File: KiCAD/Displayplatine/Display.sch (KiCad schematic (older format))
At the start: 13 parts

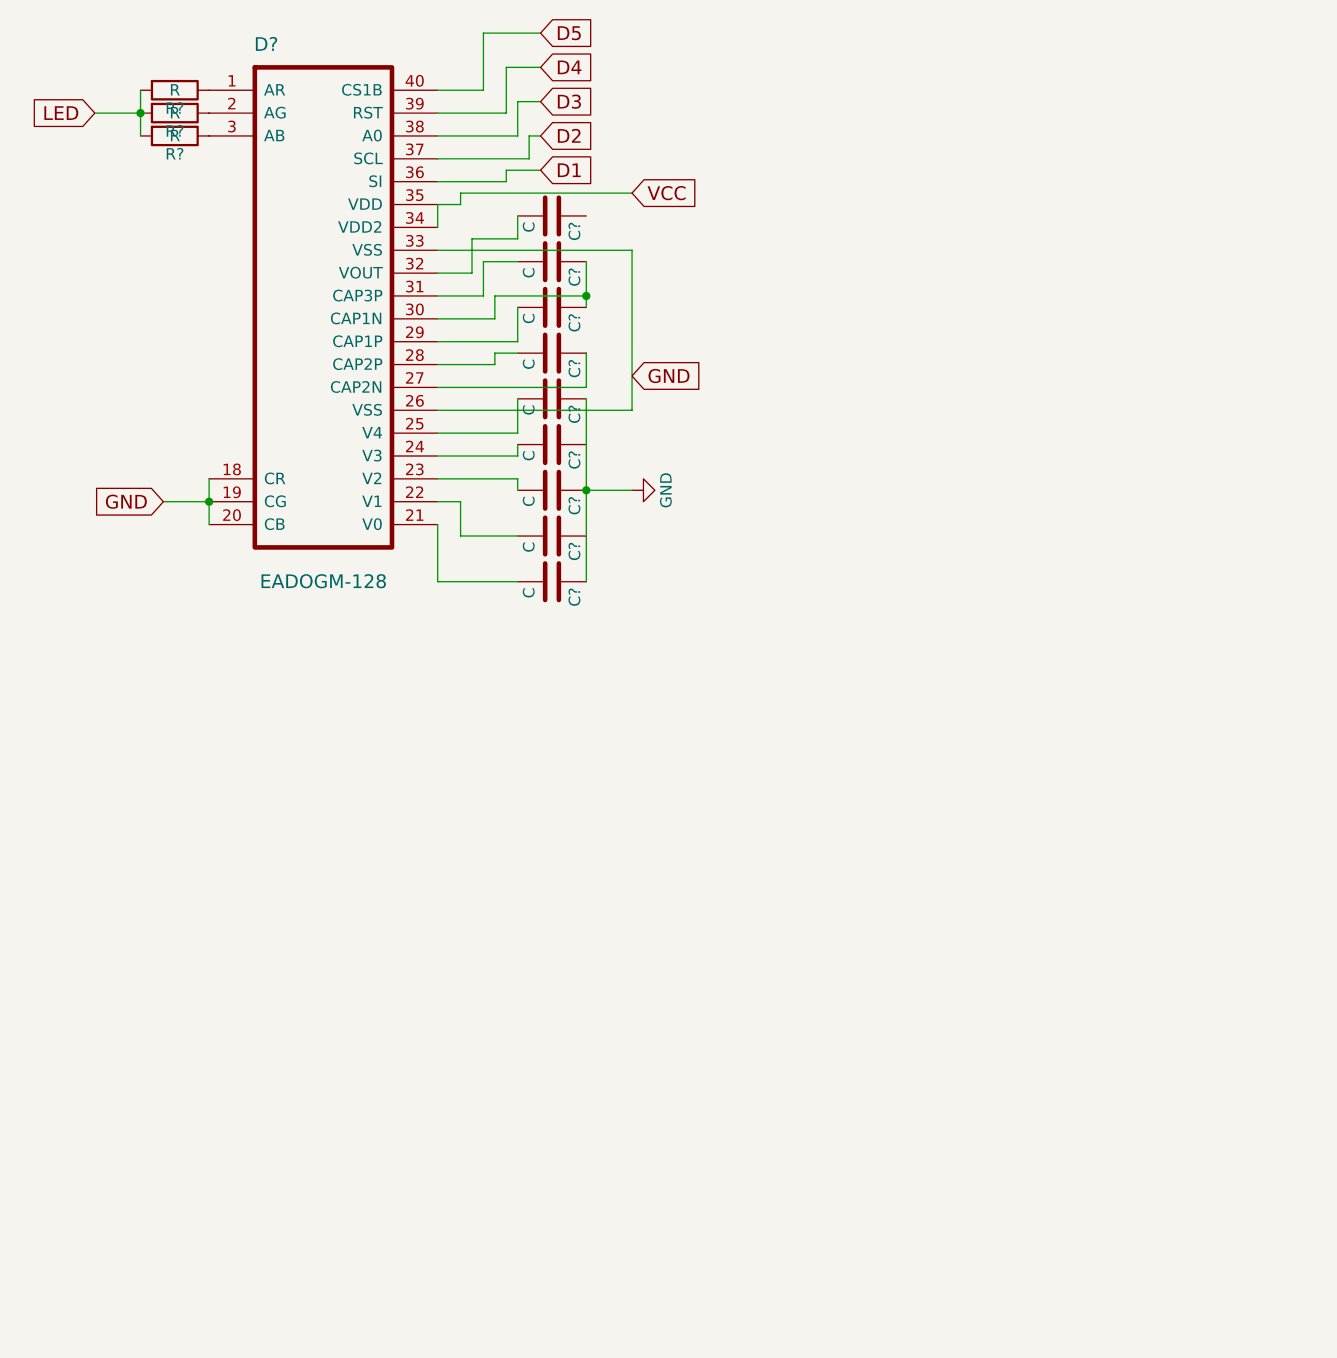
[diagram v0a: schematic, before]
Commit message: Footprints auf Displayplatine zugeordnet
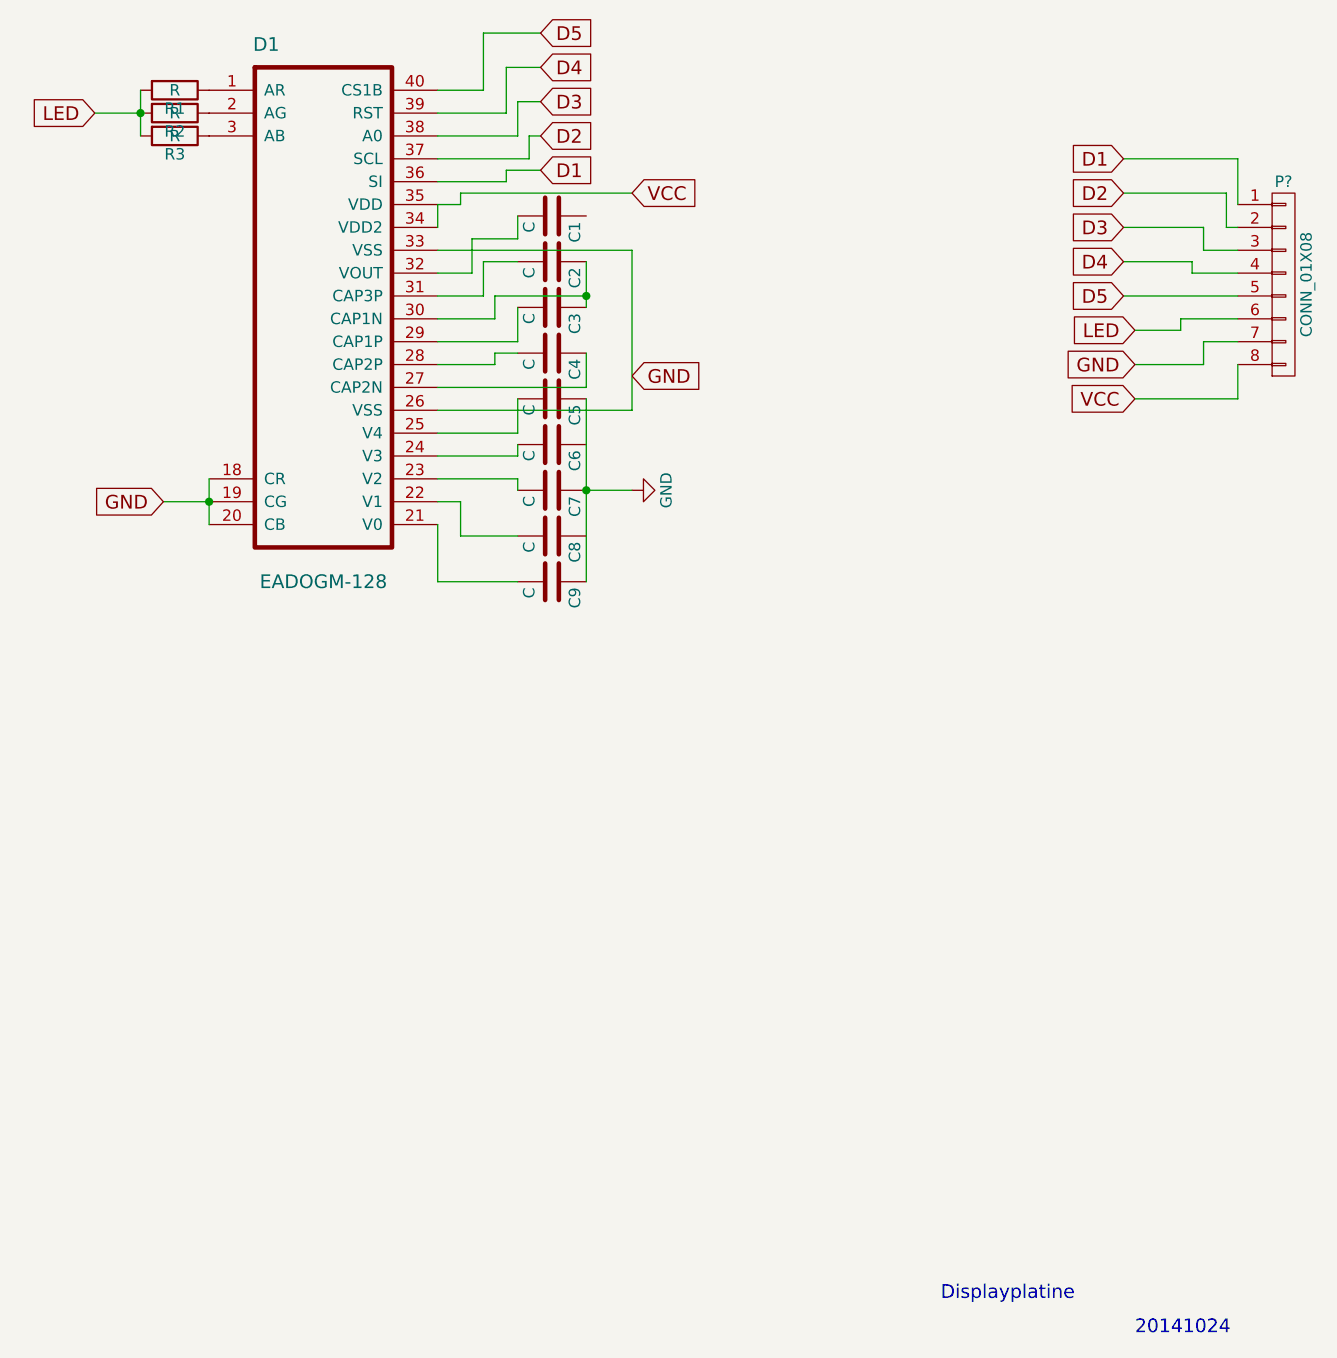
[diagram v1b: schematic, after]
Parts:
- added P?: CONN_01X08, symbol CONN_01X08
- gave numbers to parts that had none: 13
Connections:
- net D1: now also P?.1 (P1)
- net D2: now also P?.2 (P2)
- net D3: now also P?.3 (P3)
- net D4: now also P?.4 (P4)
- net D5: now also P?.5 (P5)
- net GND: now also P?.7 (P7)
- net LED: now also P?.6 (P6)
- net VCC: now also P?.8 (P8)
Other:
- note added: "20141024"
- note added: "Displayplatine"
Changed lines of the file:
@@
 LIBS:contrib
 LIBS:valves
+LIBS:Display-cache
 EELAYER 25 0
 EELAYER END
@@
 $EndDescr
 $Comp
-L EADOGM-128 D?
+L EADOGM-128 D1
 U 1 1 562B6F62
 P 4700 2800
-F 0 "D?" H 4450 3600 60  0000 C CNN
+F 0 "D1" H 4450 3600 60  0000 C CNN
 F 1 "EADOGM-128" H 4700 1250 60  0000 C CNN
 F 2 "" H 4450 3600 60  0000 C CNN
@@
 $EndComp
 $Comp
-L R R?
+L R R1
 U 1 1 562B7228
 P 4050 2200
-F 0 "R?" V 4130 2200 50  0000 C CNN
+F 0 "R1" V 4130 2200 50  0000 C CNN
 F 1 "R" V 4050 2200 50  0000 C CNN
 F 2 "" V 3980 2200 30  0000 C CNN
@@
 $EndComp
 $Comp
-L R R?
+L R R2
 U 1 1 562B727B
 P 4050 2300
-F 0 "R?" V 4130 2300 50  0000 C CNN
+F 0 "R2" V 4130 2300 50  0000 C CNN
 F 1 "R" V 4050 2300 50  0000 C CNN
 F 2 "" V 3980 2300 30  0000 C CNN
@@
 $EndComp
 $Comp
-L R R?
+L R R3
 U 1 1 562B72AC
 P 4050 2400
-F 0 "R?" V 4130 2400 50  0000 C CNN
+F 0 "R3" V 4130 2400 50  0000 C CNN
 F 1 "R" V 4050 2400 50  0000 C CNN
 F 2 "" V 3980 2400 30  0000 C CNN
@@
 $EndComp
 $Comp
-L C C?
+L C C9
 U 1 1 562B74C8
 P 5700 4350
-F 0 "C?" H 5725 4450 50  0000 L CNN
+F 0 "C9" H 5725 4450 50  0000 L CNN
 F 1 "C" H 5725 4250 50  0000 L CNN
 F 2 "" H 5738 4200 30  0000 C CNN
@@
 $EndComp
 $Comp
-L C C?
+L C C8
 U 1 1 562B7536
 P 5700 4150
-F 0 "C?" H 5725 4250 50  0000 L CNN
+F 0 "C8" H 5725 4250 50  0000 L CNN
 F 1 "C" H 5725 4050 50  0000 L CNN
 F 2 "" H 5738 4000 30  0000 C CNN
@@
 $EndComp
 $Comp
-L C C?
+L C C7
 U 1 1 562B75A3
 P 5700 3950
-F 0 "C?" H 5725 4050 50  0000 L CNN
+F 0 "C7" H 5725 4050 50  0000 L CNN
 F 1 "C" H 5725 3850 50  0000 L CNN
 F 2 "" H 5738 3800 30  0000 C CNN
@@
 $EndComp
 $Comp
-L C C?
+L C C6
 U 1 1 562B75CA
 P 5700 3750
-F 0 "C?" H 5725 3850 50  0000 L CNN
+F 0 "C6" H 5725 3850 50  0000 L CNN
 F 1 "C" H 5725 3650 50  0000 L CNN
 F 2 "" H 5738 3600 30  0000 C CNN
@@
 $EndComp
 $Comp
-L C C?
+L C C5
 U 1 1 562B7621
 P 5700 3550
-F 0 "C?" H 5725 3650 50  0000 L CNN
+F 0 "C5" H 5725 3650 50  0000 L CNN
 F 1 "C" H 5725 3450 50  0000 L CNN
 F 2 "" H 5738 3400 30  0000 C CNN
@@
 $EndComp
 $Comp
-L GND #PWR?
+L GND #PWR01
 U 1 1 562B7704
 P 6050 3950
-F 0 "#PWR?" H 6050 3700 50  0001 C CNN
+F 0 "#PWR01" H 6050 3700 50  0001 C CNN
 F 1 "GND" H 6050 3800 50  0000 C CNN
 F 2 "" H 6050 3950 60  0000 C CNN
@@
 $EndComp
 $Comp
-L C C?
+L C C4
 U 1 1 562B7CE7
 P 5700 3350
-F 0 "C?" H 5725 3450 50  0000 L CNN
+F 0 "C4" H 5725 3450 50  0000 L CNN
 F 1 "C" H 5725 3250 50  0000 L CNN
 F 2 "" H 5738 3200 30  0000 C CNN
@@
 $EndComp
 $Comp
-L C C?
+L C C3
 U 1 1 562B7D68
 P 5700 3150
-F 0 "C?" H 5725 3250 50  0000 L CNN
+F 0 "C3" H 5725 3250 50  0000 L CNN
 F 1 "C" H 5725 3050 50  0000 L CNN
 F 2 "" H 5738 3000 30  0000 C CNN
@@
 $EndComp
 $Comp
-L C C?
+L C C2
 U 1 1 562B7DB9
 P 5700 2950
-F 0 "C?" H 5725 3050 50  0000 L CNN
+F 0 "C2" H 5725 3050 50  0000 L CNN
 F 1 "C" H 5725 2850 50  0000 L CNN
 F 2 "" H 5738 2800 30  0000 C CNN
@@
 $EndComp
 $Comp
-L C C?
+L C C1
 U 1 1 562B7EAB
 P 5700 2750
-F 0 "C?" H 5725 2850 50  0000 L CNN
+F 0 "C1" H 5725 2850 50  0000 L CNN
 F 1 "C" H 5725 2650 50  0000 L CNN
 F 2 "" H 5738 2600 30  0000 C CNN
@@
 Wire Wire Line
 	5200 2900 6050 2900
+$Comp
+L CONN_01X08 P?
+U 1 1 562B950F
+P 8900 3050
+F 0 "P?" H 8900 3500 50  0000 C CNN
+F 1 "CONN_01X08" V 9000 3050 50  0000 C CNN
+F 2 "" H 8900 3050 60  0000 C CNN
+F 3 "" H 8900 3050 60  0000 C CNN
+	1    8900 3050
+	1    0    0    -1
+$EndComp
+Text GLabel 8200 2500 0    60   Input ~ 0
+D1
+Text GLabel 8200 2650 0    60   Input ~ 0
+D2
+Text GLabel 8200 2800 0    60   Input ~ 0
+D3
+Text GLabel 8200 2950 0    60   Input ~ 0
+D4
+Text GLabel 8200 3100 0    60   Input ~ 0
+D5
+Text GLabel 8250 3250 0    60   Input ~ 0
+LED
+Text GLabel 8250 3400 0    60   Input ~ 0
+GND
+Text GLabel 8250 3550 0    60   Input ~ 0
+VCC
+Wire Wire Line
+	8200 2500 8700 2500
+Wire Wire Line
+	8700 2500 8700 2700
+Wire Wire Line
+	8200 2650 8650 2650
+Wire Wire Line
+	8650 2650 8650 2800
+Wire Wire Line
+	8650 2800 8700 2800
+Wire Wire Line
+	8200 2800 8550 2800
+Wire Wire Line
+	8550 2800 8550 2900
+Wire Wire Line
+	8550 2900 8700 2900
+Wire Wire Line
+	8200 2950 8500 2950
+Wire Wire Line
+	8500 2950 8500 3000
+Wire Wire Line
+	8500 3000 8700 3000
+Wire Wire Line
+	8200 3100 8700 3100
+Wire Wire Line
+	8250 3250 8450 3250
+Wire Wire Line
+	8450 3250 8450 3200
+Wire Wire Line
+	8450 3200 8700 3200
+Wire Wire Line
+	8250 3400 8550 3400
+Wire Wire Line
+	8550 3400 8550 3300
+Wire Wire Line
+	8550 3300 8700 3300
+Wire Wire Line
+	8250 3550 8700 3550
+Wire Wire Line
+	8700 3550 8700 3400
+Text Notes 7400 7500 0    60   ~ 0
+Displayplatine
+Text Notes 8250 7650 0    60   ~ 0
+20141024
 $EndSCHEMATC

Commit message: Footprint EADOG korrigiert + Kondensatoren besserer Footprint
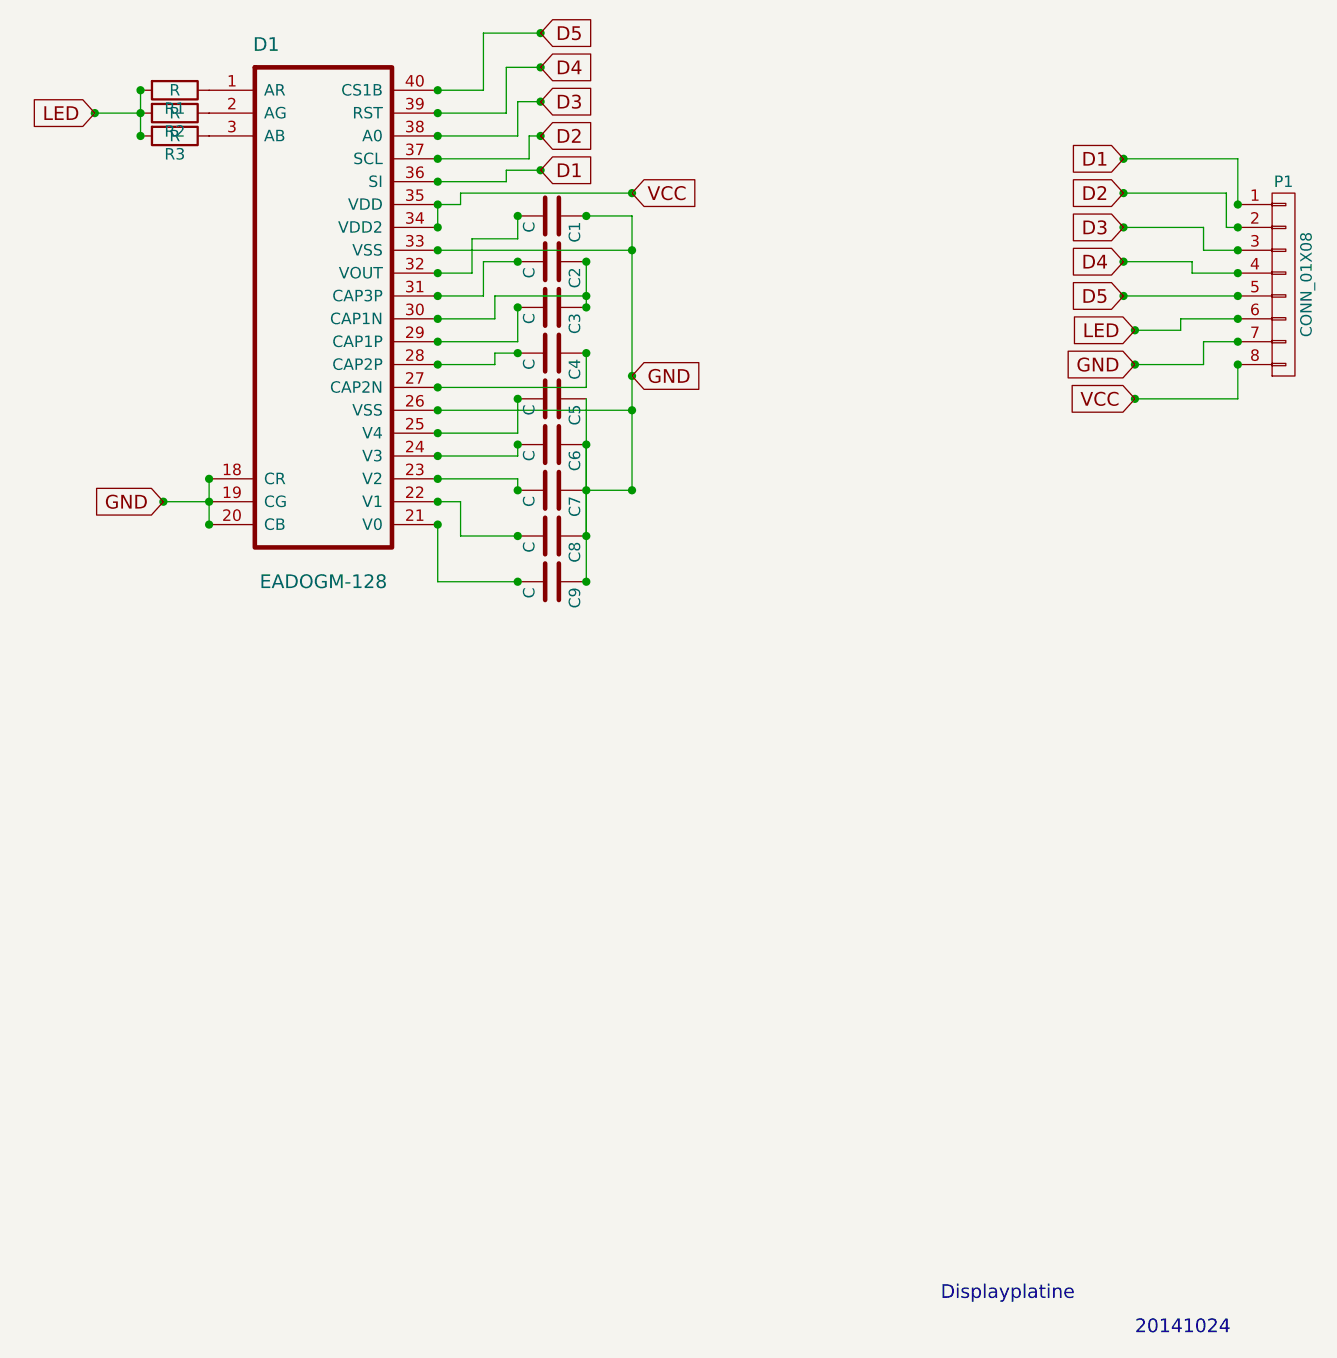
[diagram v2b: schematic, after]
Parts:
- C1, C2, C3, C4, C5, C6, C7, C8, C9: footprint (none) -> Capacitors_ThroughHole:C_Disc_D3_P2.5
- D1: footprint (none) -> Displayplatine:EADOG128
- P1: renamed from P?; footprint (none) -> Pin_Headers:Pin_Header_Straight_1x08
- R1, R2, R3: footprint (none) -> Resistors_ThroughHole:Resistor_Horizontal_RM10mm
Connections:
- net GND: now also C1.1, C6.1, C8.1
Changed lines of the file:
@@
 F 0 "D1" H 4450 3600 60  0000 C CNN
 F 1 "EADOGM-128" H 4700 1250 60  0000 C CNN
-F 2 "" H 4450 3600 60  0000 C CNN
+F 2 "Displayplatine:EADOG128" H 4450 3600 60  0001 C CNN
 F 3 "" H 4450 3600 60  0000 C CNN
 	1    4700 2800
@@
 F 0 "R1" V 4130 2200 50  0000 C CNN
 F 1 "R" V 4050 2200 50  0000 C CNN
-F 2 "" V 3980 2200 30  0000 C CNN
+F 2 "Resistors_ThroughHole:Resistor_Horizontal_RM10mm" V 3980 2200 30  0001 C CNN
 F 3 "" H 4050 2200 30  0000 C CNN
 	1    4050 2200
@@
 F 0 "R2" V 4130 2300 50  0000 C CNN
 F 1 "R" V 4050 2300 50  0000 C CNN
-F 2 "" V 3980 2300 30  0000 C CNN
+F 2 "Resistors_ThroughHole:Resistor_Horizontal_RM10mm" V 3980 2300 30  0001 C CNN
 F 3 "" H 4050 2300 30  0000 C CNN
 	1    4050 2300
@@
 F 0 "R3" V 4130 2400 50  0000 C CNN
 F 1 "R" V 4050 2400 50  0000 C CNN
-F 2 "" V 3980 2400 30  0000 C CNN
+F 2 "Resistors_ThroughHole:Resistor_Horizontal_RM10mm" V 3980 2400 30  0001 C CNN
 F 3 "" H 4050 2400 30  0000 C CNN
 	1    4050 2400
@@
 F 0 "C9" H 5725 4450 50  0000 L CNN
 F 1 "C" H 5725 4250 50  0000 L CNN
-F 2 "" H 5738 4200 30  0000 C CNN
+F 2 "Capacitors_ThroughHole:C_Disc_D3_P2.5" H 5738 4200 30  0001 C CNN
 F 3 "" H 5700 4350 60  0000 C CNN
 	1    5700 4350
@@
 F 0 "C8" H 5725 4250 50  0000 L CNN
 F 1 "C" H 5725 4050 50  0000 L CNN
-F 2 "" H 5738 4000 30  0000 C CNN
+F 2 "Capacitors_ThroughHole:C_Disc_D3_P2.5" H 5738 4000 30  0001 C CNN
 F 3 "" H 5700 4150 60  0000 C CNN
 	1    5700 4150
@@
 F 0 "C7" H 5725 4050 50  0000 L CNN
 F 1 "C" H 5725 3850 50  0000 L CNN
-F 2 "" H 5738 3800 30  0000 C CNN
+F 2 "Capacitors_ThroughHole:C_Disc_D3_P2.5" H 5738 3800 30  0001 C CNN
 F 3 "" H 5700 3950 60  0000 C CNN
 	1    5700 3950
@@
 F 0 "C6" H 5725 3850 50  0000 L CNN
 F 1 "C" H 5725 3650 50  0000 L CNN
-F 2 "" H 5738 3600 30  0000 C CNN
+F 2 "Capacitors_ThroughHole:C_Disc_D3_P2.5" H 5738 3600 30  0001 C CNN
 F 3 "" H 5700 3750 60  0000 C CNN
 	1    5700 3750
@@
 F 0 "C5" H 5725 3650 50  0000 L CNN
 F 1 "C" H 5725 3450 50  0000 L CNN
-F 2 "" H 5738 3400 30  0000 C CNN
+F 2 "Capacitors_ThroughHole:C_Disc_D3_P2.5" H 5738 3400 30  0001 C CNN
 F 3 "" H 5700 3550 60  0000 C CNN
 	1    5700 3550
 	0    1    1    0
-$EndComp
-$Comp
-L GND #PWR01
-U 1 1 562B7704
-P 6050 3950
-F 0 "#PWR01" H 6050 3700 50  0001 C CNN
-F 1 "GND" H 6050 3800 50  0000 C CNN
-F 2 "" H 6050 3950 60  0000 C CNN
-F 3 "" H 6050 3950 60  0000 C CNN
-	1    6050 3950
-	0    -1   -1   0
 $EndComp
 $Comp
@@
 F 0 "C4" H 5725 3450 50  0000 L CNN
 F 1 "C" H 5725 3250 50  0000 L CNN
-F 2 "" H 5738 3200 30  0000 C CNN
+F 2 "Capacitors_ThroughHole:C_Disc_D3_P2.5" H 5738 3200 30  0001 C CNN
 F 3 "" H 5700 3350 60  0000 C CNN
 	1    5700 3350
@@
 F 0 "C3" H 5725 3250 50  0000 L CNN
 F 1 "C" H 5725 3050 50  0000 L CNN
-F 2 "" H 5738 3000 30  0000 C CNN
+F 2 "Capacitors_ThroughHole:C_Disc_D3_P2.5" H 5738 3000 30  0001 C CNN
 F 3 "" H 5700 3150 60  0000 C CNN
 	1    5700 3150
@@
 F 0 "C2" H 5725 3050 50  0000 L CNN
 F 1 "C" H 5725 2850 50  0000 L CNN
-F 2 "" H 5738 2800 30  0000 C CNN
+F 2 "Capacitors_ThroughHole:C_Disc_D3_P2.5" H 5738 2800 30  0001 C CNN
 F 3 "" H 5700 2950 60  0000 C CNN
 	1    5700 2950
@@
 F 0 "C1" H 5725 2850 50  0000 L CNN
 F 1 "C" H 5725 2650 50  0000 L CNN
-F 2 "" H 5738 2600 30  0000 C CNN
+F 2 "Capacitors_ThroughHole:C_Disc_D3_P2.5" H 5738 2600 30  0001 C CNN
 F 3 "" H 5700 2750 60  0000 C CNN
 	1    5700 2750
@@
 	5850 3550 5850 4350
 Wire Wire Line
-	5850 3950 6050 3950
+	6050 3950 5850 3950
 Connection ~ 5850 3950
 Wire Wire Line
@@
 	6050 3600 5200 3600
 Wire Wire Line
-	6050 2900 6050 3600
+	6050 2750 6050 3950
 Wire Wire Line
 	3900 2200 3900 2400
@@
 	5200 2900 6050 2900
 $Comp
-L CONN_01X08 P?
+L CONN_01X08 P1
 U 1 1 562B950F
 P 8900 3050
-F 0 "P?" H 8900 3500 50  0000 C CNN
+F 0 "P1" H 8900 3500 50  0000 C CNN
 F 1 "CONN_01X08" V 9000 3050 50  0000 C CNN
-F 2 "" H 8900 3050 60  0000 C CNN
+F 2 "Pin_Headers:Pin_Header_Straight_1x08" H 8900 3050 60  0001 C CNN
 F 3 "" H 8900 3050 60  0000 C CNN
 	1    8900 3050
@@
 Text Notes 8250 7650 0    60   ~ 0
 20141024
+Wire Wire Line
+	5850 3750 5850 4150
+Connection ~ 5850 3750
+Connection ~ 5850 4150
+Wire Wire Line
+	5850 2750 6050 2750
+Connection ~ 6050 2900
+Connection ~ 6050 3450
+Connection ~ 5200 2700
+Connection ~ 5650 2550
+Connection ~ 6050 2650
+Connection ~ 5650 2400
+Connection ~ 5650 2250
+Connection ~ 5650 2100
+Connection ~ 5650 1950
+Connection ~ 3700 2300
+Connection ~ 3900 2200
+Connection ~ 3900 2400
+Connection ~ 4000 4000
+Connection ~ 4200 4100
+Connection ~ 4200 3900
+Connection ~ 5200 4100
+Connection ~ 5200 4000
+Connection ~ 5200 3900
+Connection ~ 5200 3800
+Connection ~ 5200 3700
+Connection ~ 5200 3600
+Connection ~ 5200 3500
+Connection ~ 5200 3400
+Connection ~ 5200 3300
+Connection ~ 5200 3200
+Connection ~ 5200 3100
+Connection ~ 5200 3000
+Connection ~ 5200 2900
+Connection ~ 5200 2800
+Connection ~ 5200 2600
+Connection ~ 5200 2500
+Connection ~ 5200 2400
+Connection ~ 5200 2300
+Connection ~ 5200 2200
+Connection ~ 8700 3400
+Connection ~ 8700 3300
+Connection ~ 8700 3200
+Connection ~ 8700 3100
+Connection ~ 8700 3000
+Connection ~ 8700 2900
+Connection ~ 8700 2800
+Connection ~ 8700 2700
+Connection ~ 8200 2500
+Connection ~ 8200 2650
+Connection ~ 8200 2800
+Connection ~ 8200 2950
+Connection ~ 8200 3100
+Connection ~ 8250 3250
+Connection ~ 8250 3400
+Connection ~ 8250 3550
+Connection ~ 6050 3950
+Connection ~ 6050 3600
+Connection ~ 5550 2750
+Connection ~ 5550 2950
+Connection ~ 5550 3150
+Connection ~ 5550 3350
+Connection ~ 5550 3550
+Connection ~ 5550 3750
+Connection ~ 5550 3950
+Connection ~ 5550 4150
+Connection ~ 5550 4350
+Connection ~ 5850 4350
+Connection ~ 5850 3350
+Connection ~ 5850 2950
+Connection ~ 5850 3150
+Connection ~ 5850 2750
 $EndSCHEMATC
